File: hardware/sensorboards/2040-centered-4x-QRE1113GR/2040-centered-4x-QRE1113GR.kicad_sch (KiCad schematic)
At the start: 14 parts, among them J1 Conn_01x10_Male, U1 QRE1113GR, U2 QRE1113GR, U3 QRE1113GR, U4 QRE1113GR

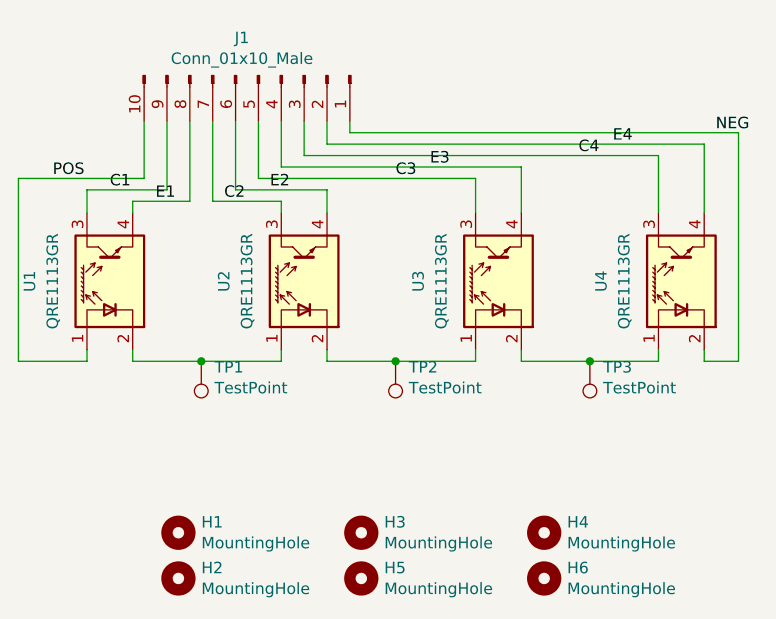
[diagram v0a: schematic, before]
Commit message: Changing the connector pins to accommodate easier PCB layout
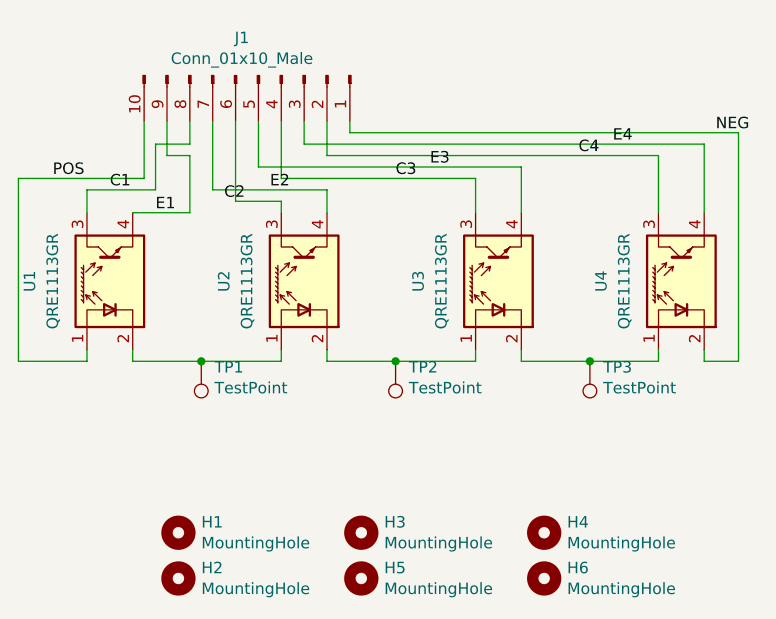
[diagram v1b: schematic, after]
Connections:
- net C1: now also J1.8 (Pin_8); no longer J1.9 (Pin_9)
- net C2: no longer J1.7 (Pin_7), U2.3
- net C3: now also J1.4 (Pin_4); no longer J1.5 (Pin_5)
- net C4: now also J1.2 (Pin_2); no longer J1.3 (Pin_3)
- net E1: now also J1.9 (Pin_9); no longer J1.8 (Pin_8)
- net E2: now also J1.7 (Pin_7); no longer J1.6 (Pin_6)
- net E3: now also J1.5 (Pin_5); no longer J1.4 (Pin_4)
- net E4: now also J1.3 (Pin_3); no longer J1.2 (Pin_2)
- new net: J1.6 (Pin_6), U2.3
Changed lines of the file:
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@@
   (junction (at 99.06 77.47) (diameter 0) (color 0 0 0 0)
   )
-  (wire (pts (xy 91.44 59.69) (xy 97.79 59.69))
-    (stroke (width 0) (type default) (color 0 0 0 0))
-  )
-  (wire (pts (xy 95.25 50.8) (xy 95.25 58.42))
-    (stroke (width 0) (type default) (color 0 0 0 0))
-  )
-  (wire (pts (xy 100.33 50.8) (xy 100.33 59.69))
+  (wire (pts (xy 91.44 60.96) (xy 97.79 60.96))
     (stroke (width 0) (type default) (color 0 0 0 0))
   )
@@
     (stroke (width 0) (type default) (color 0 0 0 0))
   )
-  (wire (pts (xy 107.95 50.8) (xy 107.95 55.88))
-    (stroke (width 0) (type default) (color 0 0 0 0))
-  )
   (wire (pts (xy 158.75 77.47) (xy 158.75 52.07))
     (stroke (width 0) (type default) (color 0 0 0 0))
   )
-  (wire (pts (xy 97.79 59.69) (xy 97.79 50.8))
+  (wire (pts (xy 129.54 57.15) (xy 107.95 57.15))
     (stroke (width 0) (type default) (color 0 0 0 0))
   )
-  (wire (pts (xy 113.03 50.8) (xy 113.03 53.34))
+  (wire (pts (xy 93.98 53.34) (xy 93.98 58.42))
     (stroke (width 0) (type default) (color 0 0 0 0))
   )
@@
     (stroke (width 0) (type default) (color 0 0 0 0))
   )
-  (wire (pts (xy 105.41 57.15) (xy 129.54 57.15))
+  (wire (pts (xy 134.62 55.88) (xy 105.41 55.88))
     (stroke (width 0) (type default) (color 0 0 0 0))
   )
   (wire (pts (xy 158.75 52.07) (xy 115.57 52.07))
-    (stroke (width 0) (type default) (color 0 0 0 0))
-  )
-  (wire (pts (xy 110.49 50.8) (xy 110.49 54.61))
     (stroke (width 0) (type default) (color 0 0 0 0))
   )
@@
     (stroke (width 0) (type default) (color 0 0 0 0))
   )
-  (wire (pts (xy 91.44 60.96) (xy 91.44 59.69))
+  (wire (pts (xy 107.95 57.15) (xy 107.95 50.8))
+    (stroke (width 0) (type default) (color 0 0 0 0))
+  )
+  (wire (pts (xy 149.86 54.61) (xy 113.03 54.61))
+    (stroke (width 0) (type default) (color 0 0 0 0))
+  )
+  (wire (pts (xy 86.36 58.42) (xy 93.98 58.42))
     (stroke (width 0) (type default) (color 0 0 0 0))
   )
   (wire (pts (xy 86.36 58.42) (xy 86.36 60.96))
+    (stroke (width 0) (type default) (color 0 0 0 0))
+  )
+  (wire (pts (xy 110.49 50.8) (xy 110.49 53.34))
     (stroke (width 0) (type default) (color 0 0 0 0))
   )
@@
     (stroke (width 0) (type default) (color 0 0 0 0))
   )
-  (wire (pts (xy 113.03 53.34) (xy 154.94 53.34))
+  (wire (pts (xy 97.79 54.61) (xy 95.25 54.61))
+    (stroke (width 0) (type default) (color 0 0 0 0))
+  )
+  (wire (pts (xy 102.87 50.8) (xy 102.87 59.69))
     (stroke (width 0) (type default) (color 0 0 0 0))
   )
@@
   )
   (wire (pts (xy 92.71 57.15) (xy 92.71 50.8))
-    (stroke (width 0) (type default) (color 0 0 0 0))
-  )
-  (wire (pts (xy 100.33 59.69) (xy 107.95 59.69))
     (stroke (width 0) (type default) (color 0 0 0 0))
   )
@@
     (stroke (width 0) (type default) (color 0 0 0 0))
   )
-  (wire (pts (xy 110.49 54.61) (xy 149.86 54.61))
-    (stroke (width 0) (type default) (color 0 0 0 0))
-  )
-  (wire (pts (xy 105.41 50.8) (xy 105.41 57.15))
-    (stroke (width 0) (type default) (color 0 0 0 0))
-  )
   (wire (pts (xy 129.54 57.15) (xy 129.54 60.96))
     (stroke (width 0) (type default) (color 0 0 0 0))
   )
-  (wire (pts (xy 107.95 55.88) (xy 134.62 55.88))
+  (wire (pts (xy 113.03 54.61) (xy 113.03 50.8))
     (stroke (width 0) (type default) (color 0 0 0 0))
   )
@@
     (stroke (width 0) (type default) (color 0 0 0 0))
   )
+  (wire (pts (xy 93.98 53.34) (xy 97.79 53.34))
+    (stroke (width 0) (type default) (color 0 0 0 0))
+  )
   (wire (pts (xy 154.94 76.2) (xy 154.94 77.47))
     (stroke (width 0) (type default) (color 0 0 0 0))
   )
   (wire (pts (xy 86.36 77.47) (xy 78.74 77.47))
+    (stroke (width 0) (type default) (color 0 0 0 0))
+  )
+  (wire (pts (xy 107.95 59.69) (xy 102.87 59.69))
+    (stroke (width 0) (type default) (color 0 0 0 0))
+  )
+  (wire (pts (xy 113.03 58.42) (xy 100.33 58.42))
+    (stroke (width 0) (type default) (color 0 0 0 0))
+  )
+  (wire (pts (xy 154.94 53.34) (xy 110.49 53.34))
     (stroke (width 0) (type default) (color 0 0 0 0))
   )
@@
     (stroke (width 0) (type default) (color 0 0 0 0))
   )
-  (wire (pts (xy 102.87 58.42) (xy 113.03 58.42))
+  (wire (pts (xy 100.33 50.8) (xy 100.33 58.42))
+    (stroke (width 0) (type default) (color 0 0 0 0))
+  )
+  (wire (pts (xy 105.41 55.88) (xy 105.41 50.8))
     (stroke (width 0) (type default) (color 0 0 0 0))
   )
@@
     (stroke (width 0) (type default) (color 0 0 0 0))
   )
-  (wire (pts (xy 95.25 58.42) (xy 86.36 58.42))
-    (stroke (width 0) (type default) (color 0 0 0 0))
-  )
-  (wire (pts (xy 102.87 50.8) (xy 102.87 58.42))
+  (wire (pts (xy 97.79 60.96) (xy 97.79 54.61))
     (stroke (width 0) (type default) (color 0 0 0 0))
   )
@@
     (stroke (width 0) (type default) (color 0 0 0 0))
   )
+  (wire (pts (xy 97.79 53.34) (xy 97.79 50.8))
+    (stroke (width 0) (type default) (color 0 0 0 0))
+  )
   (wire (pts (xy 154.94 77.47) (xy 158.75 77.47))
     (stroke (width 0) (type default) (color 0 0 0 0))
   )
   (wire (pts (xy 86.36 76.2) (xy 86.36 77.47))
+    (stroke (width 0) (type default) (color 0 0 0 0))
+  )
+  (wire (pts (xy 95.25 54.61) (xy 95.25 50.8))
     (stroke (width 0) (type default) (color 0 0 0 0))
   )
@@
     (effects (font (size 1.27 1.27)) (justify left bottom))
   )
-  (label "E1" (at 93.98 59.69 0)
+  (label "E1" (at 93.98 60.96 0)
     (effects (font (size 1.27 1.27)) (justify left bottom))
   )

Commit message: - using straight, rather than angled, connector - adjusted the board size - included 3D models - added a README and a raytracing model of the board
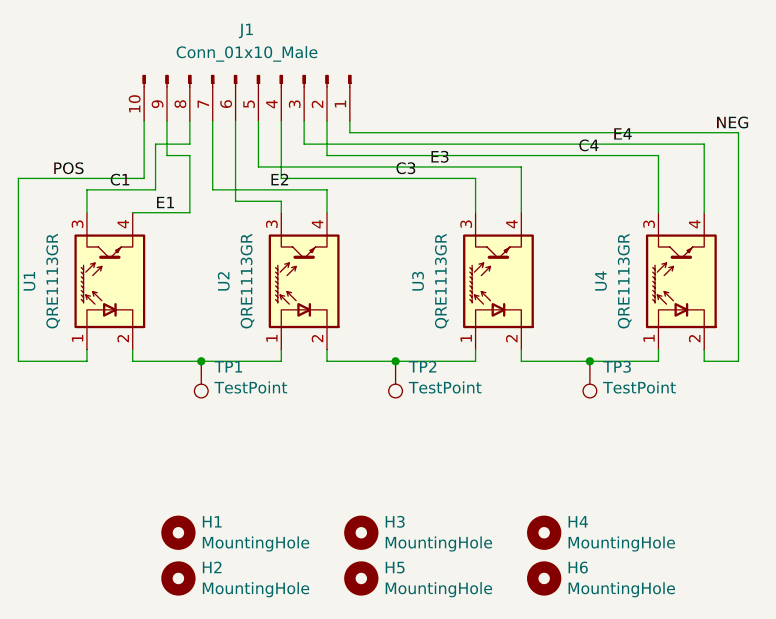
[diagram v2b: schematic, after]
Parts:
- J1: footprint Pin_Headers:Pin_Header_Angled_1x10_Pitch2.54mm -> Connector_PinHeader_2.54mm:PinHeader_1x10_P2.54mm_Vertical

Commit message: Do not populate and details on population for parts
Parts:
- H1, H2, H3, H4, H5, H6, TP1, TP2, TP3: Population (none) -> DNP
- J1: Population (none) -> Yes (through hole assembly); Short Description (none) -> Through-hole header to connect the board to other board; Vendor (none) -> generic part
- U1, U2, U3, U4: MPN (none) -> QRE1113GR; Population (none) -> Yes (SMT); Short Description (none) -> Reflective Optical Sensor; Vendor (none) -> https://www.arrow.com/en/products/qre1113gr/on-semiconductor
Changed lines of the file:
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@@
+      (effects (font (size 1.27 1.27)) hide)
+    )
+    (property "Population" "DNP" (id 4) (at 96.52 96.52 0)
       (effects (font (size 1.27 1.27)) hide)
     )
@@
       (effects (font (size 1.27 1.27)) hide)
     )
+    (property "Population" "DNP" (id 4) (at 96.52 101.6 0)
+      (effects (font (size 1.27 1.27)) hide)
+    )
   )
   (symbol (lib_id "Connector:TestPoint") (at 99.06 77.47 180) (unit 1)
@@
       (effects (font (size 1.27 1.27)) hide)
     )
+    (property "Population" "DNP" (id 4) (at 99.06 77.47 0)
+      (effects (font (size 1.27 1.27)) hide)
+    )
     (pin "1")
   )
@@
       (effects (font (size 1.27 1.27)) hide)
     )
+    (property "Population" "DNP" (id 4) (at 120.65 77.47 0)
+      (effects (font (size 1.27 1.27)) hide)
+    )
     (pin "1")
   )
@@
       (effects (font (size 1.27 1.27)) hide)
     )
+    (property "Population" "DNP" (id 4) (at 142.24 77.47 0)
+      (effects (font (size 1.27 1.27)) hide)
+    )
     (pin "1")
   )
@@
       (effects (font (size 1.27 1.27)) hide)
     )
+    (property "Population" "DNP" (id 4) (at 116.84 96.52 0)
+      (effects (font (size 1.27 1.27)) hide)
+    )
   )
   (symbol (lib_id "Mechanical:MountingHole") (at 116.84 101.6 0) (unit 1)
@@
       (effects (font (size 1.27 1.27)) hide)
     )
+    (property "Population" "DNP" (id 4) (at 116.84 101.6 0)
+      (effects (font (size 1.27 1.27)) hide)
+    )
   )
   (symbol (lib_id "Mechanical:MountingHole") (at 137.16 96.52 0) (unit 1)
@@
       (effects (font (size 1.27 1.27)) hide)
     )
+    (property "Population" "DNP" (id 4) (at 137.16 96.52 0)
+      (effects (font (size 1.27 1.27)) hide)
+    )
   )
   (symbol (lib_id "Mechanical:MountingHole") (at 137.16 101.6 0) (unit 1)
@@
     )
     (property "Datasheet" "~" (id 3) (at 137.16 101.6 0)
+      (effects (font (size 1.27 1.27)) hide)
+    )
+    (property "Population" "DNP" (id 4) (at 137.16 101.6 0)
       (effects (font (size 1.27 1.27)) hide)
     )
@@
       (effects (font (size 1.27 1.27)) hide)
     )
+    (property "MPN" "QRE1113GR" (id 4) (at 132.08 68.58 0)
+      (effects (font (size 1.27 1.27)) hide)
+    )
+    (property "Short Description" "Reflective Optical Sensor" (id 5) (at 132.08 68.58 0)
+      (effects (font (size 1.27 1.27)) hide)
+    )
+    (property "Vendor" "https://www.arrow.com/en/products/qre1113gr/on-semiconductor" (id 6) (at 132.08 68.58 0)
+      (effects (font (size 1.27 1.27)) hide)
+    )
+    (property "Population" "Yes (SMT)" (id 7) (at 132.08 68.58 0)
+      (effects (font (size 1.27 1.27)) hide)
+    )
     (pin "1")
     (pin "2")
@@
       (effects (font (size 1.27 1.27)) hide)
     )
+    (property "MPN" "QRE1113GR" (id 4) (at 152.4 68.58 0)
+      (effects (font (size 1.27 1.27)) hide)
+    )
+    (property "Vendor" "https://www.arrow.com/en/products/qre1113gr/on-semiconductor" (id 5) (at 152.4 68.58 0)
+      (effects (font (size 1.27 1.27)) hide)
+    )
+    (property "Short Description" "Reflective Optical Sensor" (id 6) (at 152.4 68.58 0)
+      (effects (font (size 1.27 1.27)) hide)
+    )
+    (property "Population" "Yes (SMT)" (id 7) (at 152.4 68.58 0)
+      (effects (font (size 1.27 1.27)) hide)
+    )
     (pin "1")
     (pin "2")
@@
       (effects (font (size 1.27 1.27)) hide)
     )
+    (property "MPN" "QRE1113GR" (id 4) (at 88.9 68.58 0)
+      (effects (font (size 1.27 1.27)) hide)
+    )
+    (property "Short Description" "Reflective Optical Sensor" (id 5) (at 88.9 68.58 0)
+      (effects (font (size 1.27 1.27)) hide)
+    )
+    (property "Vendor" "https://www.arrow.com/en/products/qre1113gr/on-semiconductor" (id 6) (at 88.9 68.58 0)
+      (effects (font (size 1.27 1.27)) hide)
+    )
+    (property "Population" "Yes (SMT)" (id 7) (at 88.9 68.58 0)
+      (effects (font (size 1.27 1.27)) hide)
+    )
     (pin "1")
     (pin "2")
@@
     )
     (property "Datasheet" "~" (id 3) (at 105.41 45.72 0)
+      (effects (font (size 1.27 1.27)) hide)
+    )
+    (property "Short Description" "Through-hole header to connect the board to other board" (id 4) (at 105.41 45.72 90)
+      (effects (font (size 1.27 1.27)) hide)
+    )
+    (property "Vendor" "generic part" (id 5) (at 105.41 45.72 90)
+      (effects (font (size 1.27 1.27)) hide)
+    )
+    (property "Population" "Yes (through hole assembly)" (id 6) (at 105.41 45.72 90)
       (effects (font (size 1.27 1.27)) hide)
     )
@@
       (effects (font (size 1.27 1.27)) hide)
     )
+    (property "MPN" "QRE1113GR" (id 4) (at 110.49 68.58 0)
+      (effects (font (size 1.27 1.27)) hide)
+    )
+    (property "Short Description" "Reflective Optical Sensor" (id 5) (at 110.49 68.58 0)
+      (effects (font (size 1.27 1.27)) hide)
+    )
+    (property "Vendor" "https://www.arrow.com/en/products/qre1113gr/on-semiconductor" (id 6) (at 110.49 68.58 0)
+      (effects (font (size 1.27 1.27)) hide)
+    )
+    (property "Population" "Yes (SMT)" (id 7) (at 110.49 68.58 0)
+      (effects (font (size 1.27 1.27)) hide)
+    )
